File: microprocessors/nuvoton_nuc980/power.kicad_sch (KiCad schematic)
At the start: 81 parts, among them J1 ADC-002-1, U11 TLV74312PDBVR, U13 TLV74318PDBVR, U2 TLV74333PDBVR, U3 TPS62A01APDDCR, U4 TLV74333PDBVR, U5 MCP6541UT-E/OT, U7 MCP6541UT-E/OT

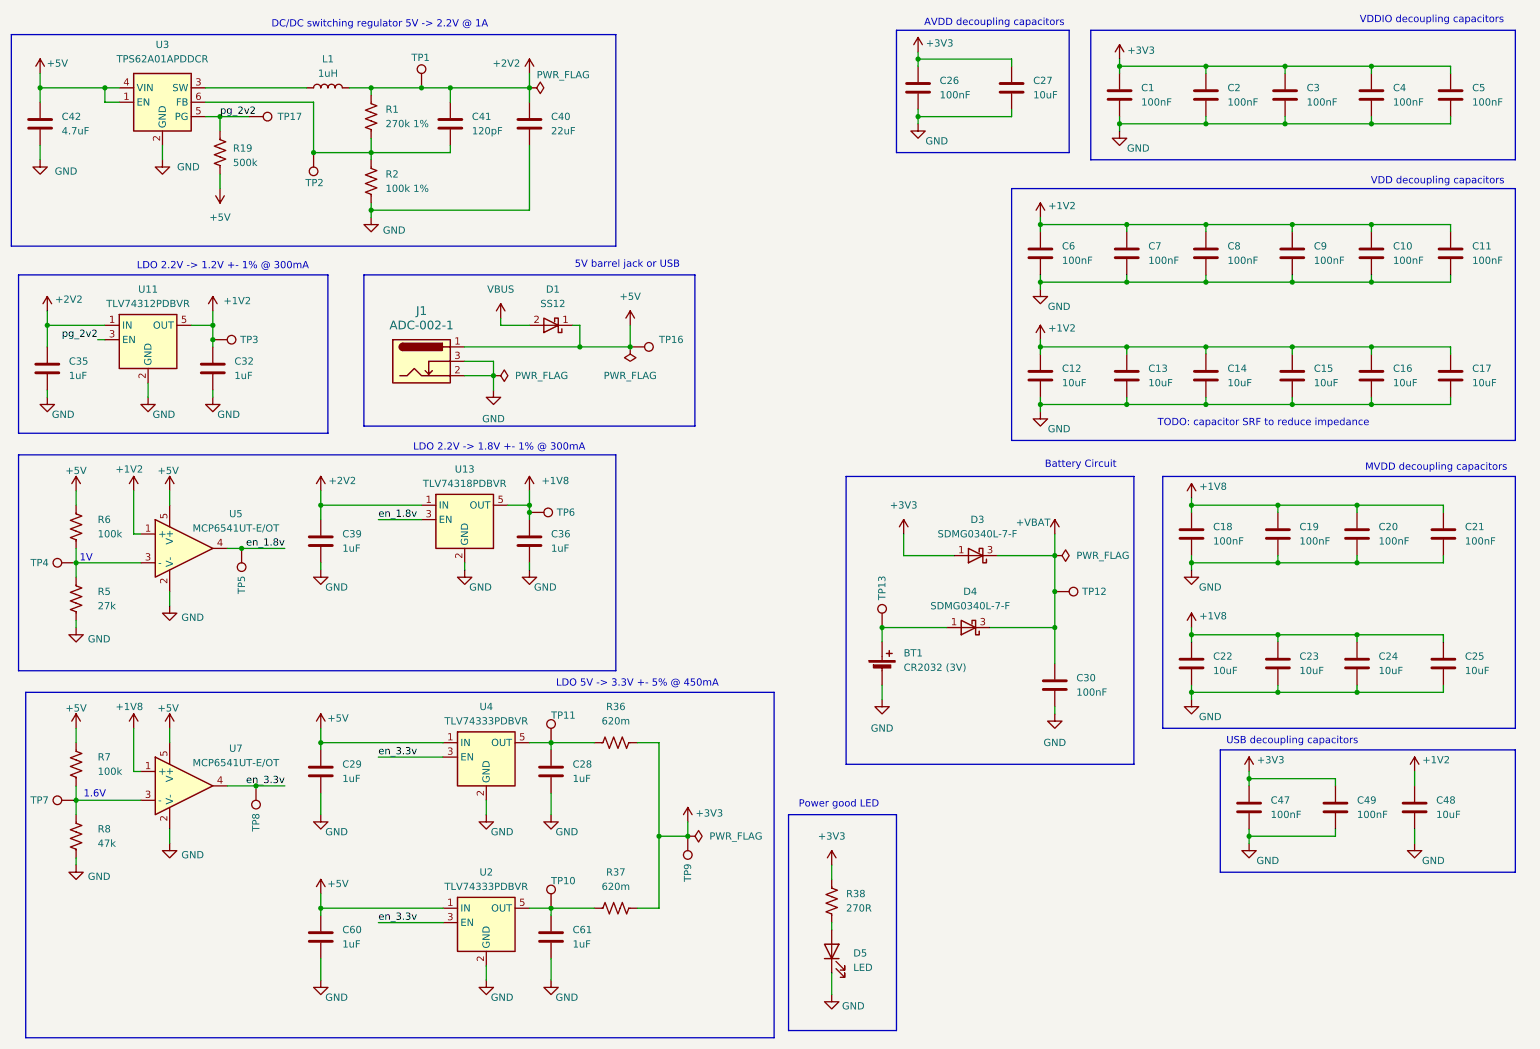
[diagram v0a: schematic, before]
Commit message: feat: ERC passing cotti-nuvoton
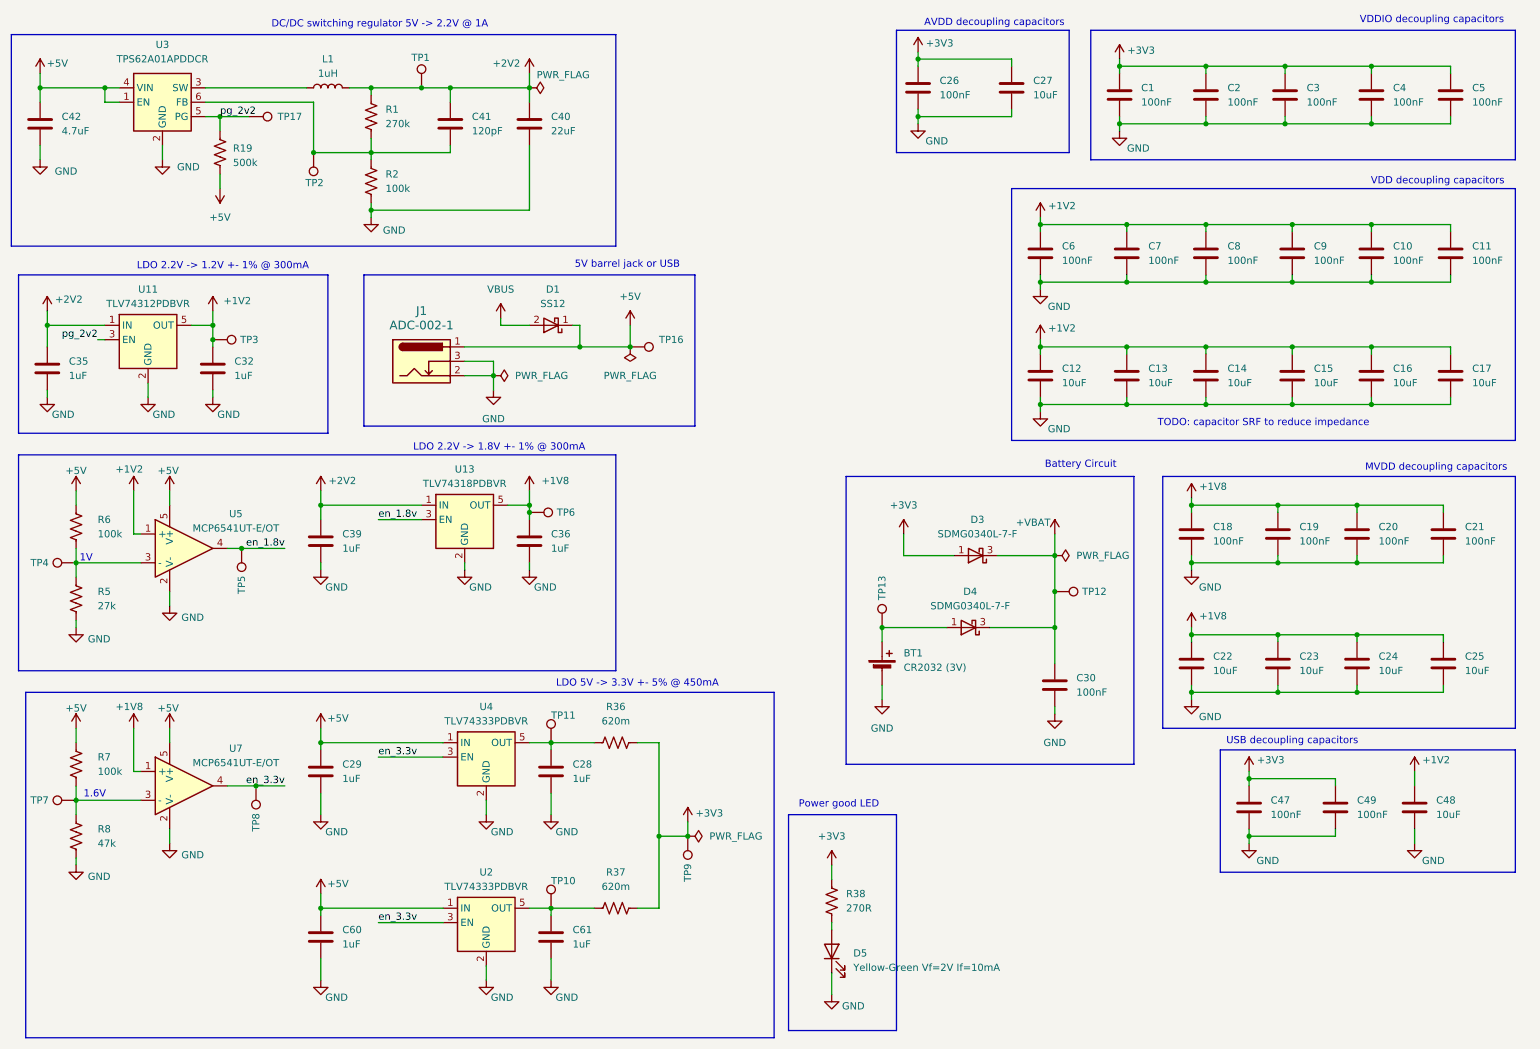
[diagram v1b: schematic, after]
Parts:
- removed BT1: CR2032 (3V), symbol Device:Battery_Cell
- removed D5: LED, symbol Device:LED
- added BT1: CR2032 (3V), cotti_footprints:BAT_BH-25C-1, symbol cotti_power:Battery_Cell_Coin_Holder
- added D5: Yellow-Green Vf=2V If=10mA, LED_SMD:LED_0603_1608Metric_Pad1.05x0.95mm_HandSolder, symbol cotti_leds:LED_Yellow_Green_SMD
- C1, C10, C11, C18, C19, C2, C20, C21, C26, C3, C30, C4, C47, C49, C5, C6, C7, C8, C9: footprint (none) -> Capacitor_SMD:C_0805_2012Metric_Pad1.18x1.45mm_HandSolder; Digikey (none) -> https://www.digikey.com/en/products/detail/samsung-electro-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; Mfr. (none) -> Samsung Electro-Mechanics; Mfr. P/N (none) -> CL21B104KACNNNC
- C12, C13, C14, C15, C16, C17, C22, C23, C24, C25, C27, C48: footprint (none) -> Capacitor_SMD:C_0805_2012Metric_Pad1.18x1.45mm_HandSolder; Digikey (none) -> https://www.digikey.com/en/products/detail/samsung-electro-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; Mfr. (none) -> Samsung Electro-Mechanics; Mfr. P/N (none) -> CL21B106KOQNNNE
- C28, C29, C32, C35, C36, C39, C60, C61: footprint (none) -> Capacitor_SMD:C_0805_2012Metric_Pad1.18x1.45mm_HandSolder; Digikey (none) -> https://www.digikey.com/en/products/detail/samsung-electro-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; Mfr. (none) -> Samsung Electro-Mechanics; Mfr. P/N (none) -> CL21B105KBFNNNE
- C40: footprint (none) -> Capacitor_SMD:C_0805_2012Metric_Pad1.18x1.45mm_HandSolder; Digikey (none) -> https://www.digikey.com/en/products/detail/samsung-electro-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; Mfr. (none) -> Samsung Electro-Mechanics; Mfr. P/N (none) -> CL21A226MAYNNNE
- C41: footprint (none) -> Capacitor_SMD:C_0805_2012Metric_Pad1.18x1.45mm_HandSolder; Digikey (none) -> https://www.digikey.com/en/products/detail/kemet/C0805C121K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; Mfr. (none) -> KEMET; Mfr. P/N (none) -> C0805C121K5HACTU
- C42: footprint (none) -> Capacitor_SMD:C_0805_2012Metric_Pad1.18x1.45mm_HandSolder; Digikey (none) -> https://www.digikey.com/en/products/detail/samsung-electro-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; Mfr. (none) -> Samsung Electro-Mechanics; Mfr. P/N (none) -> CL21A475KPFNNNE
- L1: footprint (none) -> Inductor_SMD:L_0805_2012Metric_Pad1.05x1.20mm_HandSolder; Digikey (none) -> https://www.digikey.com/en/products/detail/tdk-corporation/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; Mfr. (none) -> TDK Corporation; Mfr. P/N (none) -> MLZ2012A1R0WT000
- R1: value 270k 1% -> 270k; footprint (none) -> Resistor_SMD:R_0805_2012Metric_Pad1.20x1.40mm_HandSolder; Digikey (none) -> https://www.digikey.com/en/products/detail/yageo/RC0805FR-1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; Mfr. (none) -> YAGEO; Mfr. P/N (none) -> RC0805FR-13270KL
- R19: footprint (none) -> Resistor_SMD:R_0805_2012Metric_Pad1.20x1.40mm_HandSolder; Digikey (none) -> https://www.digikey.com/en/products/detail/yageo/RC0805FR-0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; Mfr. (none) -> YAGEO; Mfr. P/N (none) -> RC0805FR-07499KL
- R2: value 100k 1% -> 100k; footprint (none) -> Resistor_SMD:R_0805_2012Metric_Pad1.20x1.40mm_HandSolder; Digikey (none) -> https://www.digikey.com/en/products/detail/yageo/AC0805FR-1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; Mfr. (none) -> YAGEO; Mfr. P/N (none) -> AC0805FR-13100KL
- R36, R37: footprint (none) -> Resistor_SMD:R_0805_2012Metric_Pad1.20x1.40mm_HandSolder; Digikey (none) -> https://www.digikey.com/en/products/detail/bourns-inc/CRL08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; Mfr. (none) -> Bourns Inc.; Mfr. P/N (none) -> CRL0805-FW-R620ELF
- R38: footprint (none) -> Resistor_SMD:R_0805_2012Metric_Pad1.20x1.40mm_HandSolder; Digikey (none) -> https://www.digikey.com/en/products/detail/yageo/RC0805FR-1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; Mfr. (none) -> YAGEO; Mfr. P/N (none) -> RC0805FR-10270RL
- R5: footprint (none) -> Resistor_SMD:R_0805_2012Metric_Pad1.20x1.40mm_HandSolder; Digikey (none) -> https://www.digikey.com/en/products/detail/yageo/RC0805FR-1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; Mfr. (none) -> YAGEO; Mfr. P/N (none) -> RC0805FR-1327KL
- R6, R7: footprint (none) -> Resistor_SMD:R_0805_2012Metric_Pad1.20x1.40mm_HandSolder; Digikey (none) -> https://www.digikey.com/en/products/detail/yageo/AC0805FR-1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; Mfr. (none) -> YAGEO; Mfr. P/N (none) -> AC0805FR-13100KL
- R8: footprint (none) -> Resistor_SMD:R_0805_2012Metric_Pad1.20x1.40mm_HandSolder; Digikey (none) -> https://www.digikey.com/en/products/detail/yageo/RC0805FR-1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; Mfr. (none) -> YAGEO; Mfr. P/N (none) -> RC0805FR-1347KL
- TP1, TP2: value ~ -> TestPoint; footprint (none) -> TestPoint:TestPoint_Pad_D2.0mm
- TP10, TP11, TP12, TP13, TP16, TP17, TP3, TP4, TP5, TP6, TP7, TP8, TP9: footprint (none) -> TestPoint:TestPoint_Pad_D2.0mm
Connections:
- net GND: now also BT1.N (-), D5.1 (K)
- net at D4.1, TP13.1: now also BT1.P (+)
- net at R38.2: now also D5.2 (A)
